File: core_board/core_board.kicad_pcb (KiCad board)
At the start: 2 copper layers, 66 x 76.2 mm, 116 parts, among them J10 Conn_01x04_Pin, J11 Conn_01x02_Pin, J12 Conn_01x02_Pin, J13 Conn_01x04_Pin, J14 Conn_01x02_Pin, J15 Conn_01x02_Pin, J2 RJ45_LED_Shielded, J3 Conn_01x02_Pin, J4 Conn_01x04_Pin, J5 Conn_01x04_Pin, J6 Conn_01x02_Pin, J7 Conn_01x04_Pin, J8 Conn_01x04_Pin, J9 Conn_01x02_Pin, Q11 BSS138, Q13 BSS138, Q14 BSS138, Q16 BSS138, Q17 BSS138, Q18 BSS138, Q19 BSS138, Q2 BSS138, Q20 BSS138, Q21 BSS138, Q3 BSS138, Q4 BSS138, Q5 BSS138, Q6 BSS138, Q7 BSS138, Q9 BSS138, U1 AP63301WU7, U2 AP63205QWU7, U4 BD9G401EFJ-E2

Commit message: add
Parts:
- added J1: Molex_Megafit_02, MRDT_Connectors:MOLEX_MegaFit_02_Horizontal, F.Cu at (225.2, 108.1)
- added L3: 22uH, AMRM00101040220MA1:IND_AMRM00101040_PUL, F.Cu at (238.3, 106.6)
- added Q1: TPC8132_LQS, MRDT_Devices:TPC8132_LQS, F.Cu at (234.8, 117.5)
- added SW1: SW_Push, MRDT_Switches:SW_SPST_TL3305A, F.Cu at (245.9, 73.5)
- added SW2: SW_Push, MRDT_Switches:SW_SPST_TL3305A, F.Cu at (245.9, 79.6)
- added SW3: SW_Push, MRDT_Switches:SW_SPST_TL3305A, F.Cu at (245.9, 85.6)
- added SW4: SW_Push, MRDT_Switches:SW_SPST_TL3305A, F.Cu at (245.9, 91.7)
- added U3: ~, MRDT_Shields:RoveNode_H5, F.Cu at (190.8, 71.2)
- added U5: ~, MRDT_Drill_Holes:4_40_Hole_Pad_Via, F.Cu at (261.5, 110.5)
- added U6: ~, MRDT_Drill_Holes:4_40_Hole_Pad_Via, F.Cu at (261.5, 118.4)
- added U7: ~, MRDT_Drill_Holes:4_40_Hole_Pad_Via, F.Cu at (261.5, 126.4)
- added U8: ~, MRDT_Drill_Holes:4_40_Hole_Pad_Via, F.Cu at (261.5, 134.3)
- moved U2 7.43 mm to (142.2, 122.5)
- moved L1 2.06 mm to (144.0, 101.0)
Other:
- board outline removed

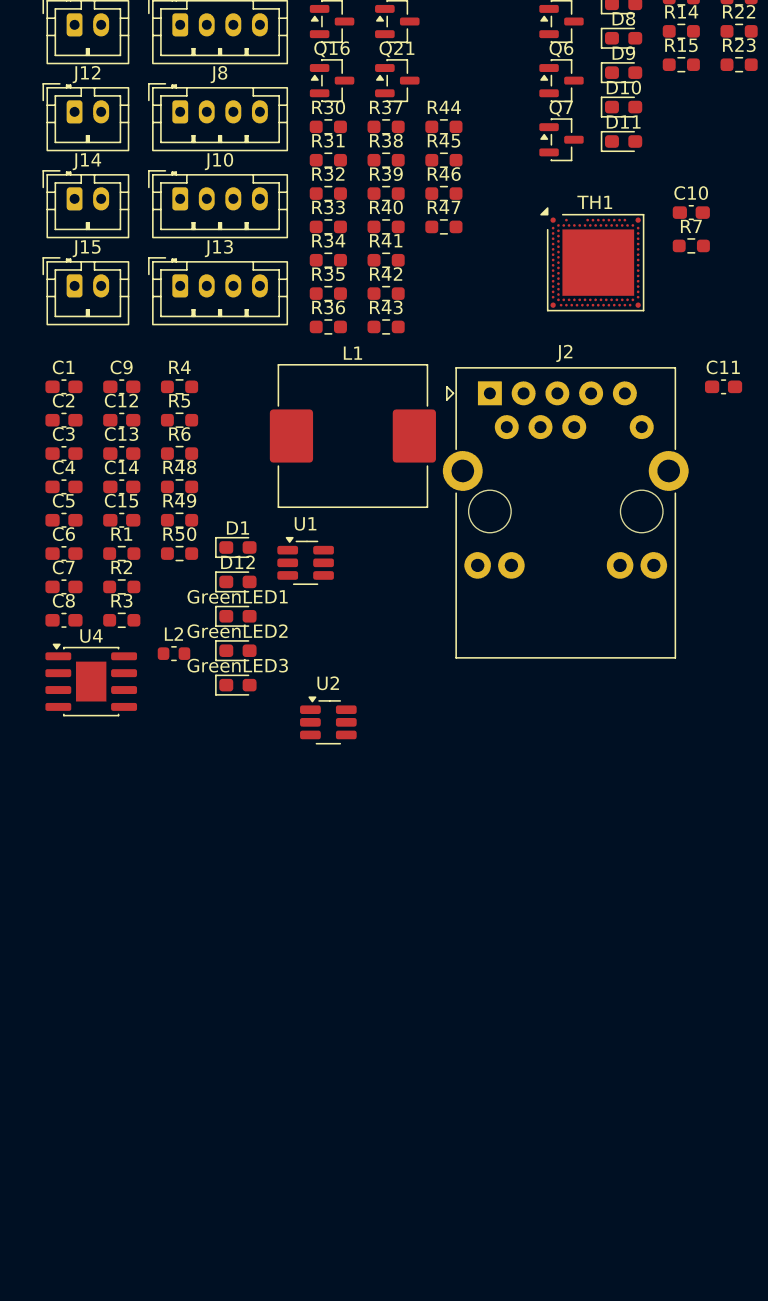
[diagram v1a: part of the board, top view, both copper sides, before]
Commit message: Add extra components
fixed LED connector
removed extra buck
fixed wrong footprints
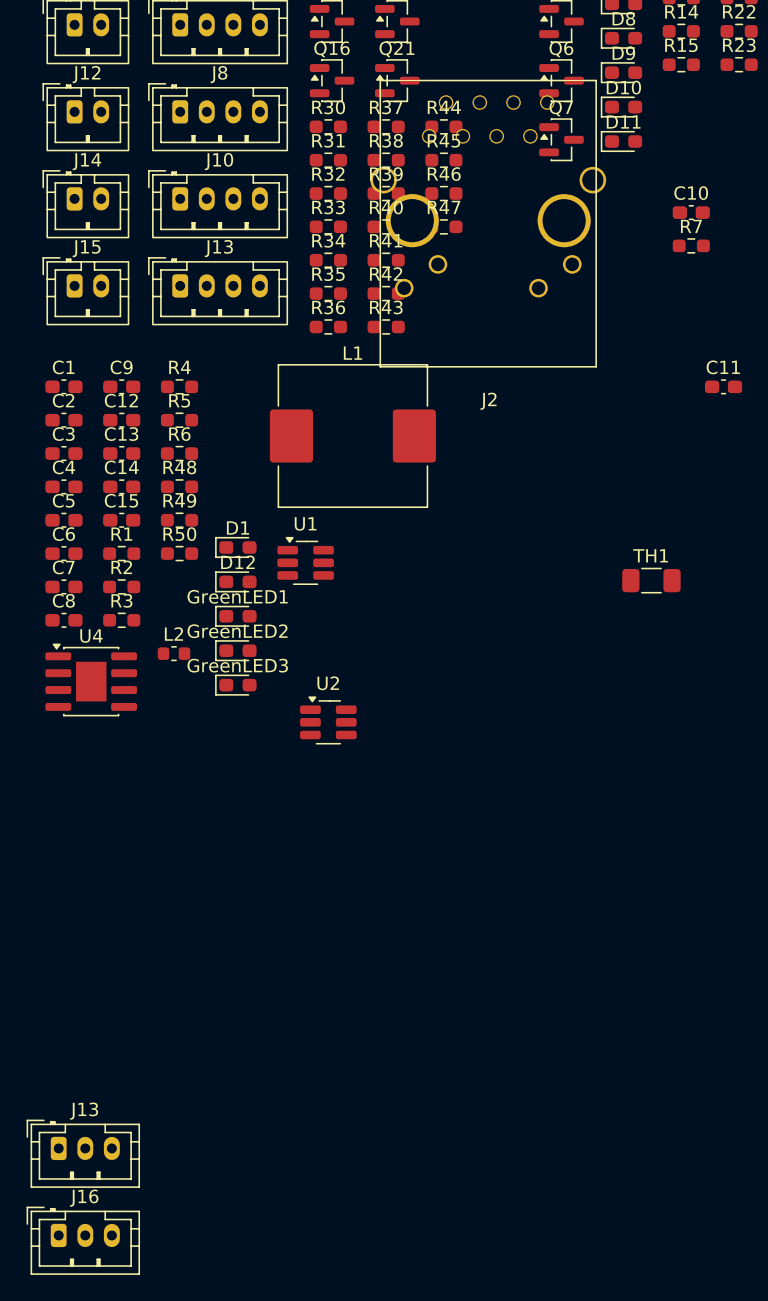
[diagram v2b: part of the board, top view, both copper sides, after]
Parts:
- added J13: Conn_01x03_Pin, Connector_JST:JST_PH_B3B-PH-K_1x03_P2.00mm_Vertical, F.Cu at (121.9, 154.6)
- added J16: Conn_01x03_Pin, Connector_JST:JST_PH_B3B-PH-K_1x03_P2.00mm_Vertical, F.Cu at (121.9, 161.2)
- J2: footprint Connector_RJ:RJ45_Abracon_ARJP11A-MA_Horizontal -> MRDT_Connectors:RJ45_Teensy
- TH1: footprint Package_DFN_QFN:Nordic_AQFN-94-1EP_7x7mm_P0.4mm -> Resistor_SMD:R_1206_3216Metric_Pad1.30x1.75mm_HandSolder
- moved TH1 24.3 mm to (166.5, 111.9)
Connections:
- J14 pad 1: /Connectors/CANLow2 -> /Connectors/CANLow
- J14 pad 2: /Connectors/CANHigh2 -> /Connectors/CANHigh
- R44 pad 1: /electromagnet -> /Connectors/electromagnet
- U3 pad 10: /Connectors/BLUE_PWM_Internal -> unconnected-(U3-PA10-Pad10)
- U3 pad 11: /Connectors/GREEN_PWM_Internal -> unconnected-(U3-PA9-Pad11)
- U3 pad 12: /Connectors/RED_PWM_Internal -> unconnected-(U3-PA8-Pad12)
- U3 pad 13: /Connectors/RED_PWM_StateDisplay -> /Connectors/Spare1
- U3 pad 14: /Connectors/BLUE_PWM_StateDisplay -> /Connectors/InternalLighting_PWM
- U3 pad 15: /Connectors/GREEN_PWM_StateDisplay -> /Connectors/StateDisplay_PWM
- U3 pad 17: /Microcontroller/electromagnet -> /Connectors/electromagnet

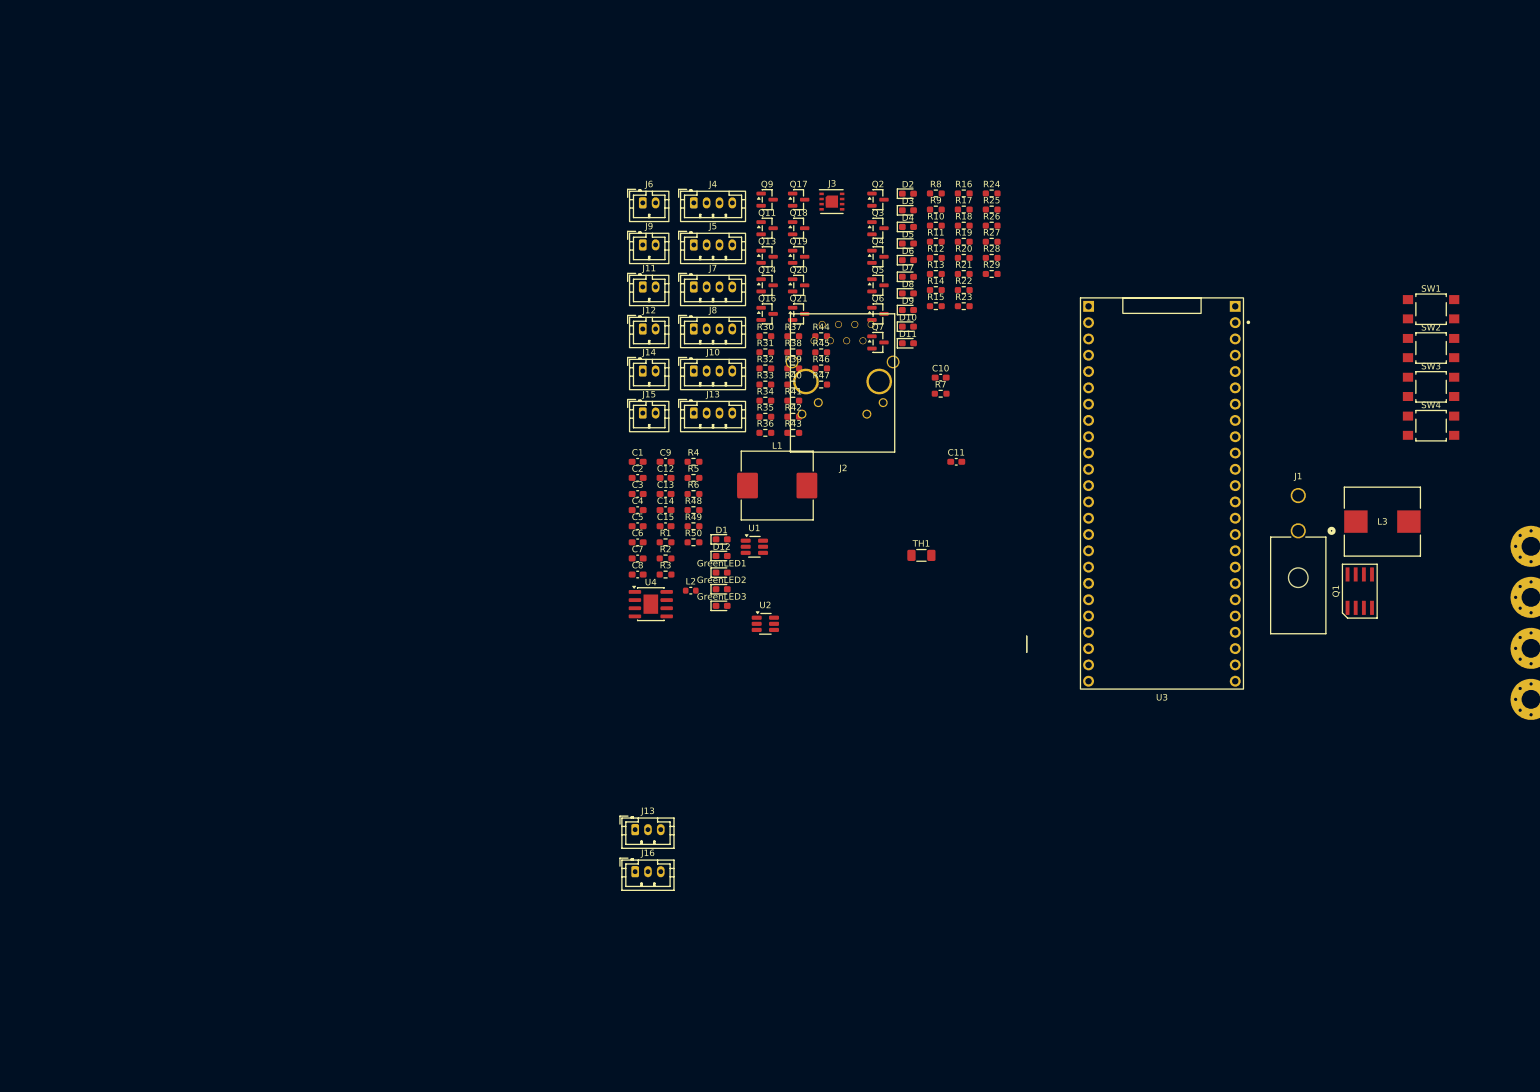
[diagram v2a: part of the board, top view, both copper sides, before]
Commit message: Started layout
started a basic layout
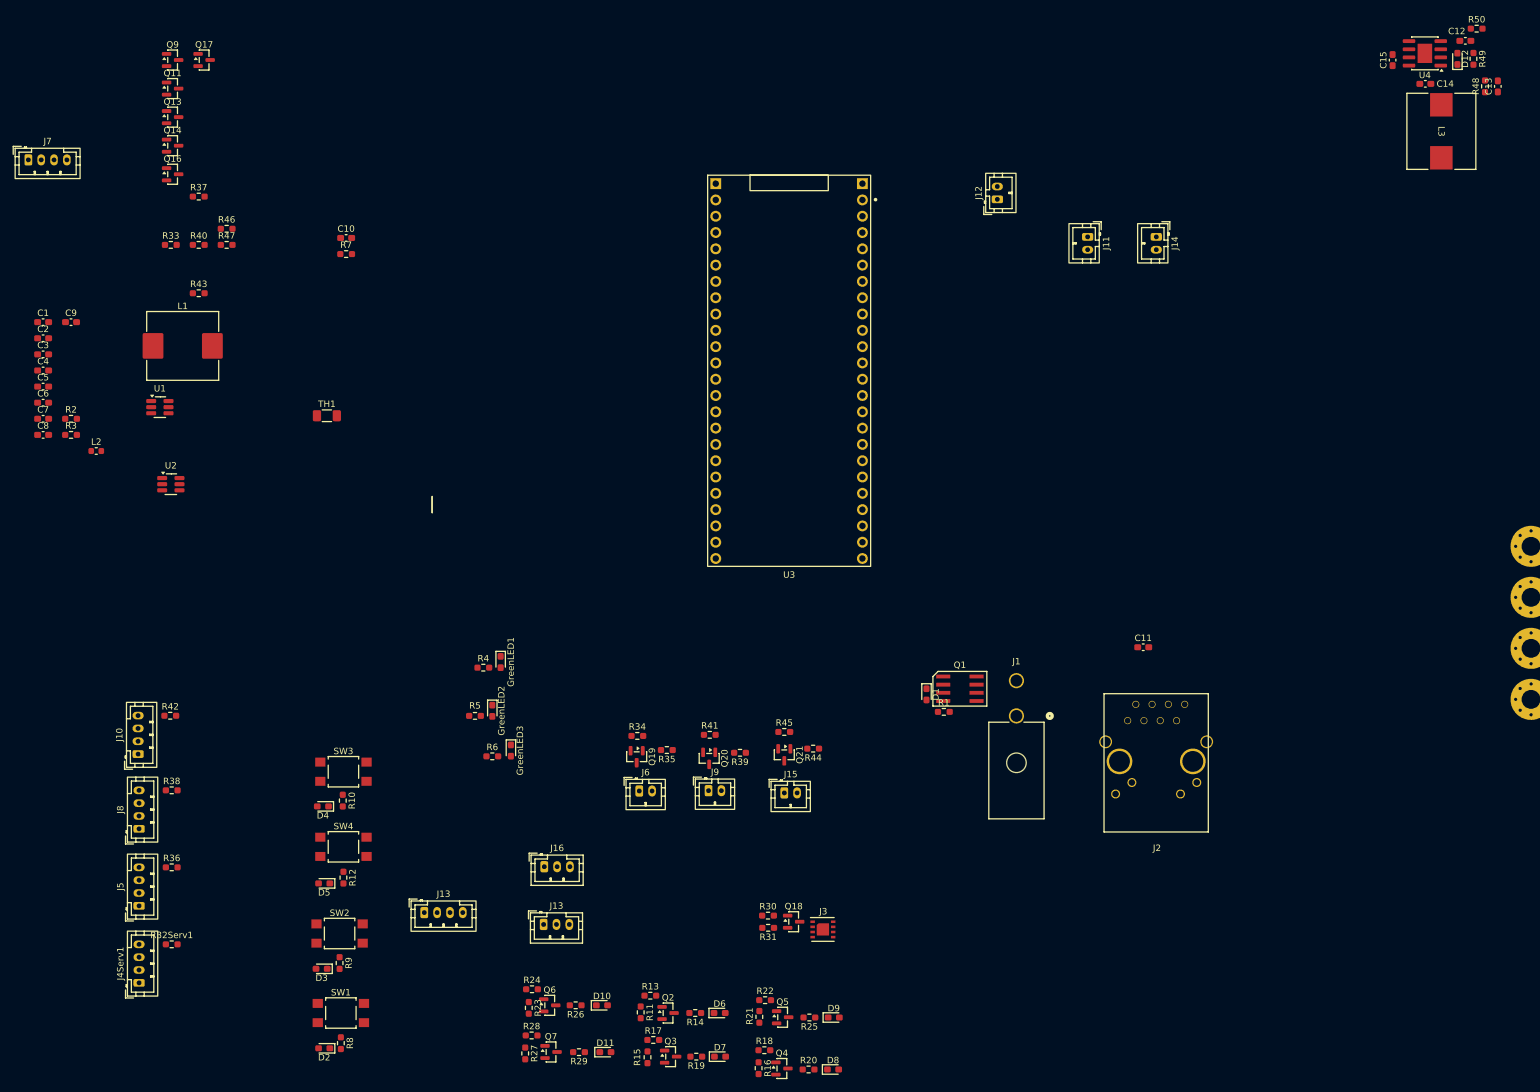
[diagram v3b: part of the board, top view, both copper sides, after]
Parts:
- moved SW1 202.2 mm to (76.0, 183.2)
- moved SW2 193.0 mm to (75.8, 170.8)
- moved SW4 181.8 mm to (76.4, 157.3)
- moved SW3 179.8 mm to (76.4, 145.6)
- moved R8 161.7 mm to (76.0, 187.9), turned to -90 degrees
- moved D2 161.3 mm to (73.4, 188.7), turned to 180 degrees
- moved R9 149.7 mm to (75.8, 175.4), turned to -90 degrees
- moved D3 149.4 mm to (73.0, 176.3), turned to 180 degrees
- moved J4Serv1 149.2 mm to (44.5, 178.5), turned to 90 degrees
- moved U4 148.1 mm to (244.9, 33.6), turned to 180 degrees
- moved R50 146.0 mm to (253.0, 29.8)
- moved R27 145.9 mm to (104.7, 189.5), turned to -90 degrees
- moved C13 144.4 mm to (256.3, 38.8), turned to 90 degrees
- moved R24 143.2 mm to (105.8, 179.5)
- moved C12 142.0 mm to (251.2, 31.7)
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- renumbered J4 to J4Serv1, R32 to R32Serv1

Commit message: add
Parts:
- removed C2: 10uF, Capacitor_SMD:C_0603_1608Metric_Pad1.08x0.95mm_HandSolder
- removed C4: 100nF, Capacitor_SMD:C_0603_1608Metric_Pad1.08x0.95mm_HandSolder
- removed C6, C7: 22uF, Capacitor_SMD:C_0603_1608Metric_Pad1.08x0.95mm_HandSolder
- removed the J13 at (89.0, 167.6)
- removed J7: Conn_01x04_Pin, Connector_JST:JST_PH_B4B-PH-K_1x04_P2.00mm_Vertical
- removed L2: 4.7uH, Inductor_SMD:L_0603_1608Metric
- removed Q11, Q13, Q14, Q16, Q17, Q9: BSS138, Package_TO_SOT_SMD:SOT-23
- removed R33, R37, R40, R43, R46, R47: 10K, Resistor_SMD:R_0603_1608Metric_Pad0.98x0.95mm_HandSolder
- removed U2: AP63205QWU7, Package_TO_SOT_SMD:SOT-23-6_Handsoldering
- added S1: 94HBB08T, 94HBBBO6T:DIPS762W56P254L991H597Q6N, F.Cu at (163.8, 55.4)
- J1: footprint MRDT_Connectors:MOLEX_MegaFit_02_Horizontal -> MRDT_Connectors:MOLEX_MegaFit_02_Vertical
- J3: footprint Converter_DCDC:Converter_DCDC_Cyntec_MUN12AD01-SH -> Connector_JST:JST_PH_B2B-PH-K_1x02_P2.00mm_Vertical
- moved U8 204.8 mm to (87.3, 26.6)
- moved U7 171.3 mm to (90.8, 141.8)
- moved C12 164.2 mm to (108.9, 113.7)
- moved C13 164.2 mm to (114.0, 120.8)
- moved C14 164.2 mm to (102.7, 120.4)
- moved C15 164.2 mm to (97.6, 116.7)
- moved D12 164.2 mm to (107.7, 116.5)
- moved L3 164.2 mm to (105.2, 127.8)
- moved R48 164.2 mm to (112.0, 120.8)
- moved R49 164.2 mm to (110.2, 116.5)
- moved R50 164.2 mm to (110.7, 111.8)
- moved U4 164.2 mm to (102.6, 115.6)
- moved D2 148.4 mm to (165.1, 72.0), turned to 90 degrees
- moved R8 147.4 mm to (167.2, 72.1), turned to 90 degrees
- moved D5 145.6 mm to (186.2, 71.0), turned to -90 degrees
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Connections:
- net Net-(U1-BST) renamed /Power/BST
- net Net-(U1-SW) renamed /Power/SW
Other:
- board text added: "PCB Editor"

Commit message: Rough draft layout
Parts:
- moved C15 110.3 mm to (184.5, 48.9), turned to 0 degrees
- moved R48 108.1 mm to (181.4, 38.0), turned to 0 degrees
- moved U4 102.8 mm to (184.7, 53.8), turned to 90 degrees
- moved C14 101.9 mm to (179.9, 53.9), turned to -90 degrees
- moved J13 98.8 mm to (147.4, 30.0)
- moved L3 98.2 mm to (172.5, 56.4), turned to 180 degrees
- moved D12 95.5 mm to (183.8, 58.9), turned to 0 degrees
- moved C12 94.4 mm to (186.6, 60.1), turned to -90 degrees
- moved R3 93.8 mm to (188.1, 41.6), turned to 180 degrees
- moved R50 93.8 mm to (188.8, 59.9), turned to 90 degrees
- moved R2 93.2 mm to (188.1, 43.4), turned to 0 degrees
- moved R49 92.0 mm to (183.8, 61.4), turned to 0 degrees
- moved J16 89.5 mm to (136.5, 30.2)
- moved C5 88.8 mm to (186.2, 45.9), turned to 180 degrees
- moved C1 86.3 mm to (183.9, 39.9), turned to 180 degrees
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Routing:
- added copper zone on B.Cu, net GND
- added copper zone on F.Cu, net GND
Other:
- board outline added: 101.6 x 113.2 mm

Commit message: rough layout
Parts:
- moved U6 1.24 mm to (189.4, 123.4)
- moved U8 0.40 mm to (111.1, 26.6)
- moved U5 0.37 mm to (189.4, 26.6)
- moved U7 0.07 mm to (111.1, 123.4)
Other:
- board size 101.6 x 113.2 mm -> 85.5 x 104 mm
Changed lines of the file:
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@@
 	(footprint "MRDT_Drill_Holes:4_40_Hole_Pad_Via"
 		(layer "F.Cu")
-		(at 189.09 26.67)
+		(at 189.444 26.556)
 		(property "Reference" "U5"
 			(at 0 -0.5 0)
@@
 	(footprint "MRDT_Drill_Holes:4_40_Hole_Pad_Via"
 		(layer "F.Cu")
-		(at 190.677944 123.577944)
+		(at 189.444 123.444)
 		(property "Reference" "U6"
 			(at 0 -0.5 0)
@@
 	(footprint "MRDT_Drill_Holes:4_40_Hole_Pad_Via"
 		(layer "F.Cu")
-		(at 111.125 123.45)
+		(at 111.056 123.444)
 		(property "Reference" "U7"
 			(at 0 -0.5 0)
@@
 	(footprint "MRDT_Drill_Holes:4_40_Hole_Pad_Via"
 		(layer "F.Cu")
-		(at 110.9 26.925)
+		(at 111.056 26.556)
 		(property "Reference" "U8"
 			(at 0 -0.5 0)
@@
 		)
 	)
-	(gr_rect
-		(start 93.568944 26.925)
-		(end 195.168944 26.925)
+	(gr_arc
+		(start 107.5 26.556)
+		(mid 108.541528 24.041528)
+		(end 111.056 23)
 		(stroke
 			(width 0.05)
 			(type default)
 		)
-		(fill no)
 		(layer "Edge.Cuts")
 	)
-	(gr_rect
-		(start 110.985 23.12)
-		(end 110.985 124.72)
+	(gr_line
+		(start 107.5 123.444)
+		(end 107.5 26.556)
 		(stroke
 			(width 0.05)
 			(type default)
 		)
-		(fill no)
 		(layer "Edge.Cuts")
 	)
-	(gr_rect
-		(start 111.125 123.45)
-		(end 116.84 123.45)
+	(gr_line
+		(start 111.056 23)
+		(end 189.444 23)
 		(stroke
 			(width 0.05)
 			(type default)
 		)
-		(fill no)
 		(layer "Edge.Cuts")
 	)
-	(gr_rect
-		(start 111.125 123.45)
-		(end 190.677944 123.577944)
+	(gr_arc
+		(start 111.056 127)
+		(mid 108.541528 125.958472)
+		(end 107.5 123.444)
 		(stroke
 			(width 0.05)
 			(type default)
 		)
-		(fill no)
 		(layer "Edge.Cuts")
 	)
 	(gr_rect
-		(start 111.526856 34.717344)
-		(end 111.526856 136.317344)
+		(start 189.09 26.67)
+		(end 189.883972 26.67)
 		(stroke
 			(width 0.05)
@@
 		(layer "Edge.Cuts")
 	)
-	(gr_rect
-		(start 189.09 26.67)
-		(end 189.09 102.87)
+	(gr_arc
+		(start 189.444 23)
+		(mid 191.958472 24.041528)
+		(end 193 26.556)
 		(stroke
 			(width 0.05)
 			(type default)
 		)
-		(fill no)
 		(layer "Edge.Cuts")
 	)
-	(gr_rect
-		(start 189.09 26.67)
-		(end 189.883972 26.67)
+	(gr_line
+		(start 189.444 127)
+		(end 111.056 127)
 		(stroke
 			(width 0.05)
 			(type default)
 		)
-		(fill no)
 		(layer "Edge.Cuts")
 	)
-	(gr_rect
-		(start 189.09 26.67)
-		(end 190.677944 123.577944)
+	(gr_line
+		(start 193 26.556)
+		(end 193 123.444)
 		(stroke
 			(width 0.05)
 			(type default)
 		)
-		(fill no)
 		(layer "Edge.Cuts")
 	)
-	(gr_rect
-		(start 190.677944 98.177944)
-		(end 190.677944 123.577944)
+	(gr_arc
+		(start 193 123.444)
+		(mid 191.958472 125.958472)
+		(end 189.444 127)
 		(stroke
 			(width 0.05)
 			(type default)
 		)
-		(fill no)
 		(layer "Edge.Cuts")
 	)

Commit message: Fix Smoco power connector
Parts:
- J12: footprint Connector_JST:JST_PH_B2B-PH-K_1x02_P2.00mm_Vertical -> MRDT_Connectors:MOLEX_MegaFit_02_Vertical
- moved J12 15.2 mm to (126.7, 72.0), turned to 0 degrees
- renumbered TH1 to THe1
